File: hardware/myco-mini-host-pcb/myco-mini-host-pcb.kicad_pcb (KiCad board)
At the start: 2 copper layers, 53.5 x 138.4 mm, 38 parts, among them J1 Conn_01x17_Female, J2 Conn_01x17_Female, Q1 AO3401A, Q2 AO3401A, Q3 AO3401A, Q4 AO3401A, SW1 DM-04-V, SW2 TS-1187A-B-A-B, U1 XC9145B33CMR-G, U2 SHT41-AD1B-R2, U3 BH1750FVI-TR, U4 MAX40203AUK+T

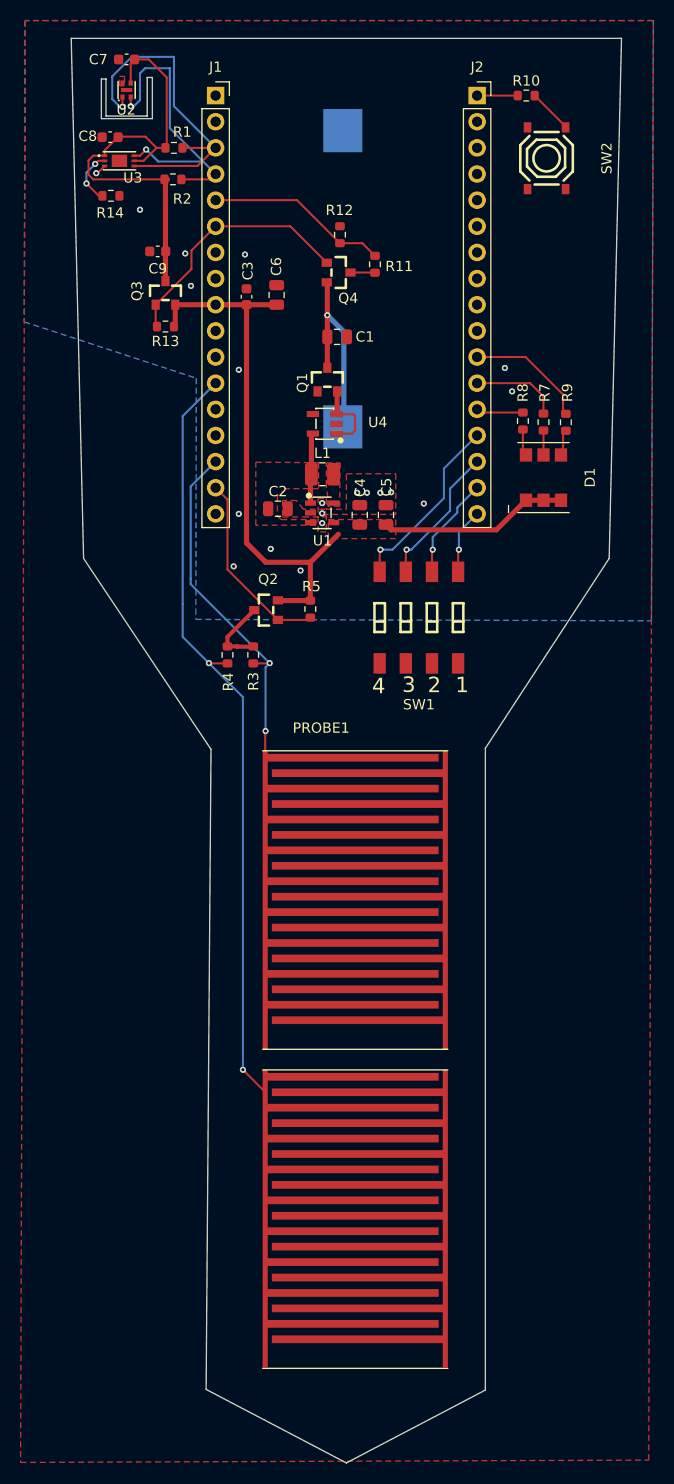
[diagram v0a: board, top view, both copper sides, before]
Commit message: feat: v1.0.0 - host PCB routé, DRC clean, prêt fab JLCPCB
- Routage complet par l'utilisateur (placement, guard zone soil probe,
  teardrops, trou de fixation gauche)
- Corrections issues de la review Opus 5 finale : dimensions du slit
  d'isolation thermique U2 mises à la spec (1.05mm uniforme sur les
  3 bras), pastilles paste/mask retirées sur U2 (SHT40) et U3 (BH1750)
  pour leurs pads die-exposée, resync librairie<->instances PCB
  (SW1 modèle 3D, BT1 attr smd, courtoisies F.CrtYd manquantes sur
  SW1/SW2/U4)
- 3 vias de la sonde sol passés en plugged+capped (IPC-4761)
- BOM : références LCSC vérifiées et prix réels pour tous les passifs
- DRC final : 0 violation, 0 unconnected
- Ajout docs/cost-tracking.md (suivi des coûts réels host PCB +
  breakout + composants, synchronisé sur le wiki GitHub)
- Datasheets BH1750 et Sensirion (SHT4x) ajoutés à misc/
- .gitignore : exclusion des exports générés (gerbers JLCPCB, rendus
  SVG temporaires) qui ne sont pas du code source

Co-Authored-By: Claude Sonnet 5 <noreply@anthropic.com>
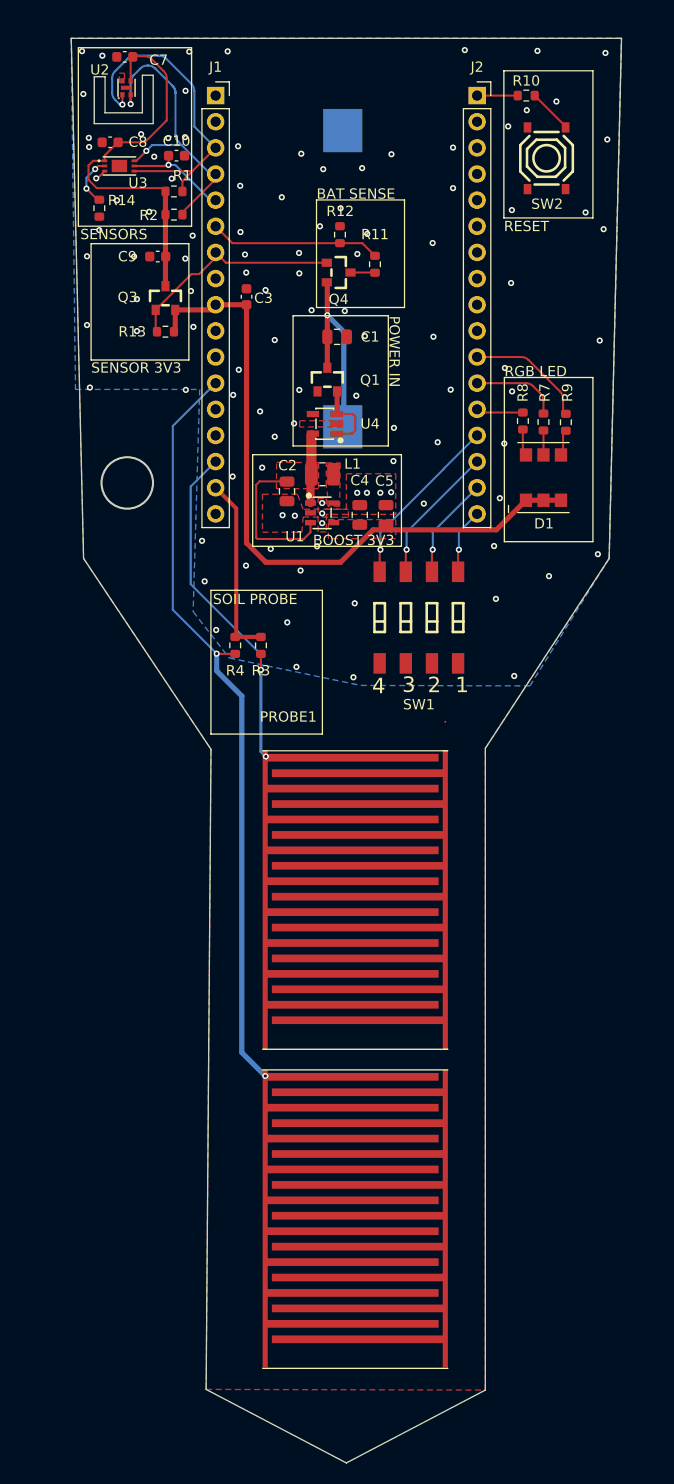
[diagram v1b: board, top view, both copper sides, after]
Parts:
- removed C6: 100uF, Capacitor_SMD:C_0805_2012Metric
- removed Q2: AO3401A, myco_host:SOT-23_L2.9-W1.3-P1.90-LS2.4-BR
- removed R5: 100k, Resistor_SMD:R_0603_1608Metric
- added C10: 100nF, Capacitor_SMD:C_0603_1608Metric, F.Cu at (61.2, 31.9)
- U2: value SHT41-AD1B-R2 -> SHT40-AD1B-R2
- moved R1 4.23 mm to (61.0, 35.4)
- moved R2 3.43 mm to (61.0, 37.6)
- moved C2 1.90 mm to (72.0, 64.5), turned to -90 degrees
- moved R14 1.64 mm to (53.8, 37.0), turned to -90 degrees
- moved R3 1.19 mm to (69.5, 79.5)
- moved R4 1.19 mm to (67.0, 79.5)
- moved C8 0.50 mm to (54.8, 30.6)
- moved C9 0.50 mm to (59.4, 41.7)
- moved Q3 0.50 mm to (60.2, 45.7)
- moved R13 0.50 mm to (60.2, 49.0)
- moved U3 0.50 mm to (55.7, 32.9)
- moved C7 0.31 mm to (56.2, 22.3)
- moved U2 0.22 mm to (56.4, 25.3)
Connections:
- J1 pad 5: /P1_12_BAT_SENSE -> /P1_12_BH_DVI
- J1 pad 6: /P1_13_SENSOR_EN -> /P1_13_BAT_SENSE
- J1 pad 7: unconnected-(J1-Pin_7-Pad7) -> /P1_14_SENSOR_EN
- Q3 pad 1: /P1_13_SENSOR_EN -> /P1_14_SENSOR_EN
- Q4 pad 1: /P1_13_SENSOR_EN -> /P1_14_SENSOR_EN
- R11 pad 2: /P1_12_BAT_SENSE -> /P1_13_BAT_SENSE
- R12 pad 1: /P1_12_BAT_SENSE -> /P1_13_BAT_SENSE
- R13 pad 2: /P1_13_SENSOR_EN -> /P1_14_SENSOR_EN
- R3 pad 1: /SOIL_VCC -> /P1_08_SOIL_SW
- R4 pad 1: /SOIL_VCC -> /P1_08_SOIL_SW
- U3 pad 5: /SENSOR_3V3 -> /P1_12_BH_DVI
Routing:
- net /P1_13_SENSOR_EN: track 24.5 -> 0.00 mm
- net /P1_14_SENSOR_EN: track 0.00 -> 21.1 mm
- net /P1_12_BAT_SENSE: track 17.7 -> 0.00 mm
- net /P1_13_BAT_SENSE: track 0.00 -> 16.3 mm
- net /BOOST_IN: track 6.85 -> 21.6 mm
- net /P1_07_SOIL_ADC1: track 48.6 -> 34.2 mm
- net /P1_04_SOIL_ADC2: track 85.6 -> 74.6 mm
- net /P1_12_BH_DVI: track 0.00 -> 10.5 mm, vias 0 -> 1
- net /SOIL_VCC: track 7.14 -> 0.00 mm
- net /VOUT_3V3: track 71.3 -> 66.6 mm
- net /SENSOR_3V3: track 43.6 -> 38.9 mm
- net /P1_11_SCL: track 30.6 -> 29.0 mm
- net /P1_10_SDA: track 33.6 -> 32.2 mm
- net /P1_08_SOIL_SW: track 18.6 -> 17.9 mm
- net /P2_03_DIP3: track 17.8 -> 17.2 mm
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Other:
- outline, holes or cut-outs redrawn
- board text added: "BAT SENSE"
- board text added: "BOOST 3V3"
- board text added: "POWER IN"
- board text added: "RESET"
- board text added: "RGB LED"
- board text added: "SENSOR 3V3"
- board text added: "SENSORS"
- board text added: "SOIL PROBE"
